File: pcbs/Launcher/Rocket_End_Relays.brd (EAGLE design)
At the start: 100 x 80 mm, 39 parts, among them IC2 LM2576T-ADJ, K4 LD105, K5 LD105, K6 LD105, K7 LD105, T1 BC547, T2 BC547, T3 BC547, T4 BC547, T5 BC547, U1 ARDUINO-MEGAPRO-5V, X1 22-23-2041, X2 22-23-2041, X3 22-23-2021, X4 22-23-2021, X5 22-23-2021, X7 22-23-2021

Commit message: * Added Arduino code for launcher code
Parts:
- R10: device resistor:0207/7 -> rcl:0207/7
- R13, R14: device rcl:0204/5 -> resistor:0207/7
- moved X4 25.4 mm to (52.1, 20.3)
- moved R3 11.5 mm to (63.5, 14.0)
- moved R13 6.35 mm to (8.89, 20.3), turned to 180 degrees
- moved C4 4.02 mm to (7.62, 14.0), turned to 270 degrees
- moved C3 2.84 mm to (8.89, 57.1), turned to 90 degrees
- moved X5 2.54 mm to (26.7, 17.8), turned to 270 degrees
- moved R14 1.27 mm to (11.4, 14.0)
- turned R10 to 270 degrees
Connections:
- removed net N$28: U1.5V@1, X1.3, X2.3
- net N$23: now also R12.2, U1.5V@1, X1.3, X2.3; no longer R12.1, T5.3
- net N$26: now also R12.1, T5.3; no longer R10.2, T5.1
- net N$31: now also R10.2
- net N$33: now also T5.1
- net N$5: no longer R12.2
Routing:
- net N$23: track 11.2 -> 57.0 mm, vias 0 -> 2
- net N$28: track 43.8 -> 0.00 mm
- net N$15: track 60.1 -> 34.7 mm
- net N$17: track 62.2 -> 39.7 mm
- net N$26: track 7.34 -> 16.9 mm
- net N$33: track 324.6 -> 315.2 mm, vias 6 -> 8
- net N$29: track 49.8 -> 44.5 mm
- net N$37: track 49.5 -> 44.2 mm
- net N$31: track 11.8 -> 15.6 mm
- net N$3: track 26.7 -> 23.4 mm
- net N$5: track 195.3 -> 192.7 mm
- net N$30: track 25.6 -> 24.2 mm
- net VCC: track 110.7 -> 111.4 mm

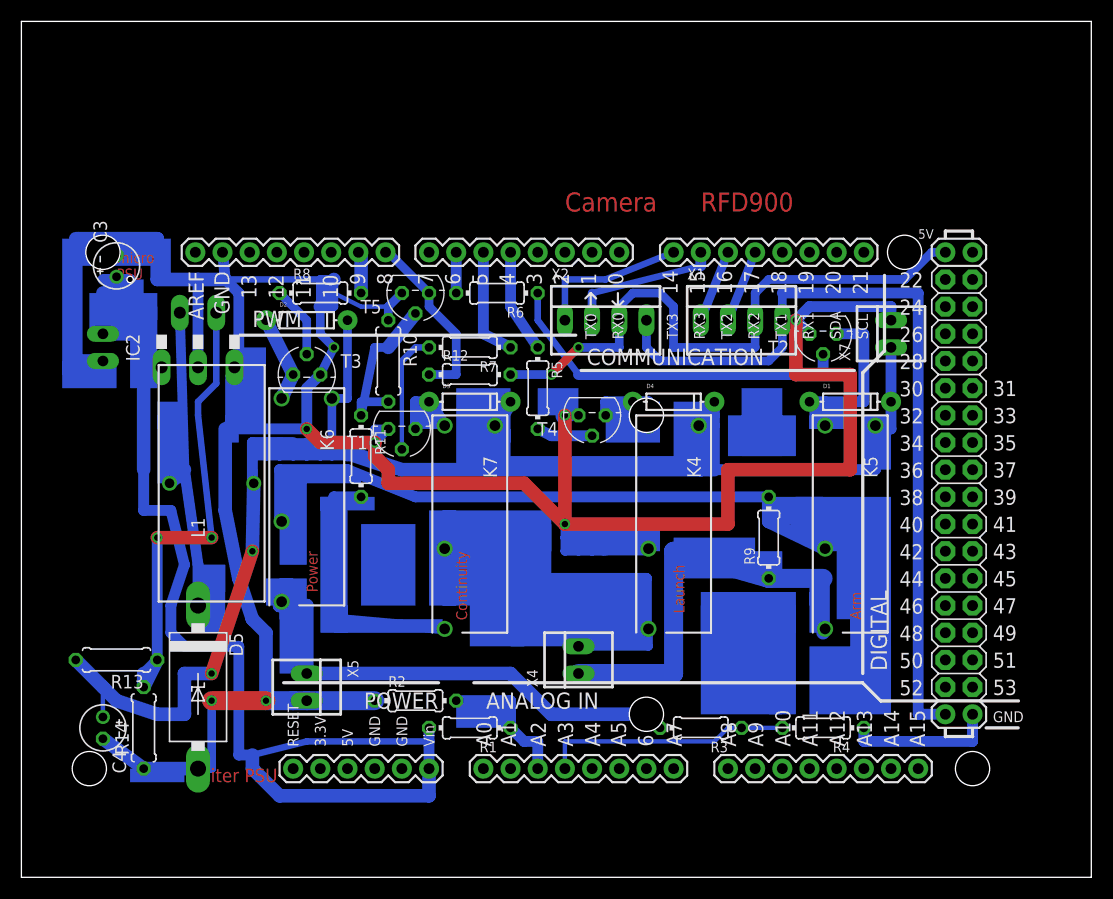
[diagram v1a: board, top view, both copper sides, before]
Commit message: * Cleaning up board with curved tracks * Putting in two screw in terminal blocks for Igniter PSU   and wires to igniter!
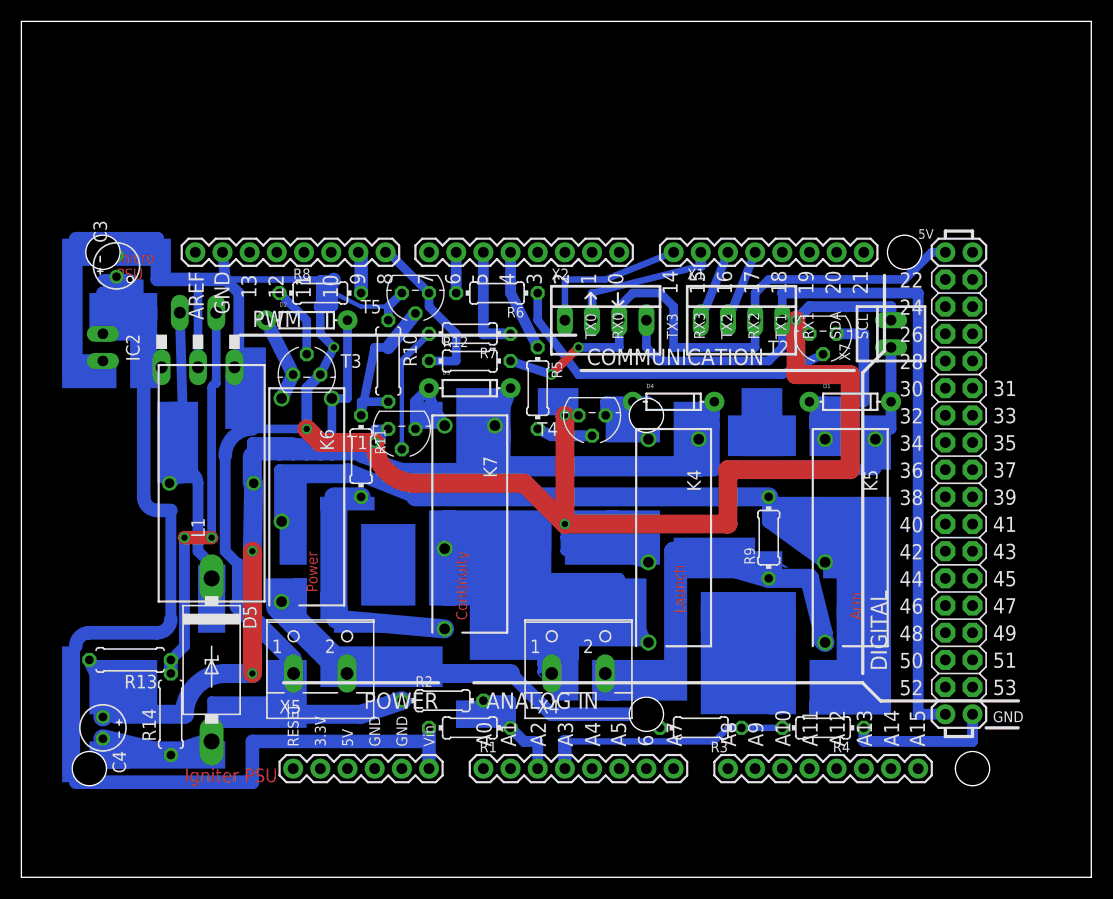
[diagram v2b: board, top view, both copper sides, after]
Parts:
- X4, X5: value 22-23-2021 -> (none); device con-molex:22-23-2021 -> con-wago-500:W237-102
- moved R14 2.84 mm to (14.0, 15.2)
- moved D5 2.84 mm to (17.8, 20.3)
- moved X5 2.84 mm to (27.9, 20.3), turned to 0 degrees
- moved R2 2.54 mm to (39.4, 16.5)
- moved K4 1.27 mm to (61.0, 31.8)
- moved K5 1.27 mm to (77.5, 31.8)
- moved R13 1.27 mm to (10.2, 20.3)
- moved D3 1.27 mm to (41.9, 45.7)
- moved R12 1.27 mm to (41.9, 48.3)
- moved R7 1.27 mm to (41.9, 50.8)
- turned X4 to 0 degrees
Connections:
- net N$15: now also X4.1; no longer X4.2
- net N$17: now also X4.2; no longer X4.1
- net N$29: now also X5.2; no longer X5.1
- net N$33: now also X5.1; no longer X5.2
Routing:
- net N$37: track 44.2 -> 37.0 mm
- net N$28: track 0.00 -> 4.86 mm
- net N$29: track 44.5 -> 40.8 mm
- net N$17: track 39.7 -> 37.1 mm
- net N$5: track 192.7 -> 195.3 mm
- net N$7: track 13.2 -> 10.7 mm
- net N$20: track 6.57 -> 8.19 mm
- net N$36: track 29.4 -> 27.8 mm
- net N$10: track 33.7 -> 32.2 mm
- net N$33: track 315.2 -> 313.9 mm, vias 8 -> 5
- net N$26: track 16.9 -> 15.6 mm
- net N$22: track 17.7 -> 18.9 mm
- net N$19: track 7.50 -> 8.77 mm
- net N$15: track 34.7 -> 33.8 mm
- net VCC: track 111.4 -> 112.1 mm
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- added copper zone on layer 16, net N$35
- added copper zone on layer 16, net N$38
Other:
- board text removed: "Camera"
- board text removed: "RFD900"

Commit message: * Labelling added to screw terminal blocks
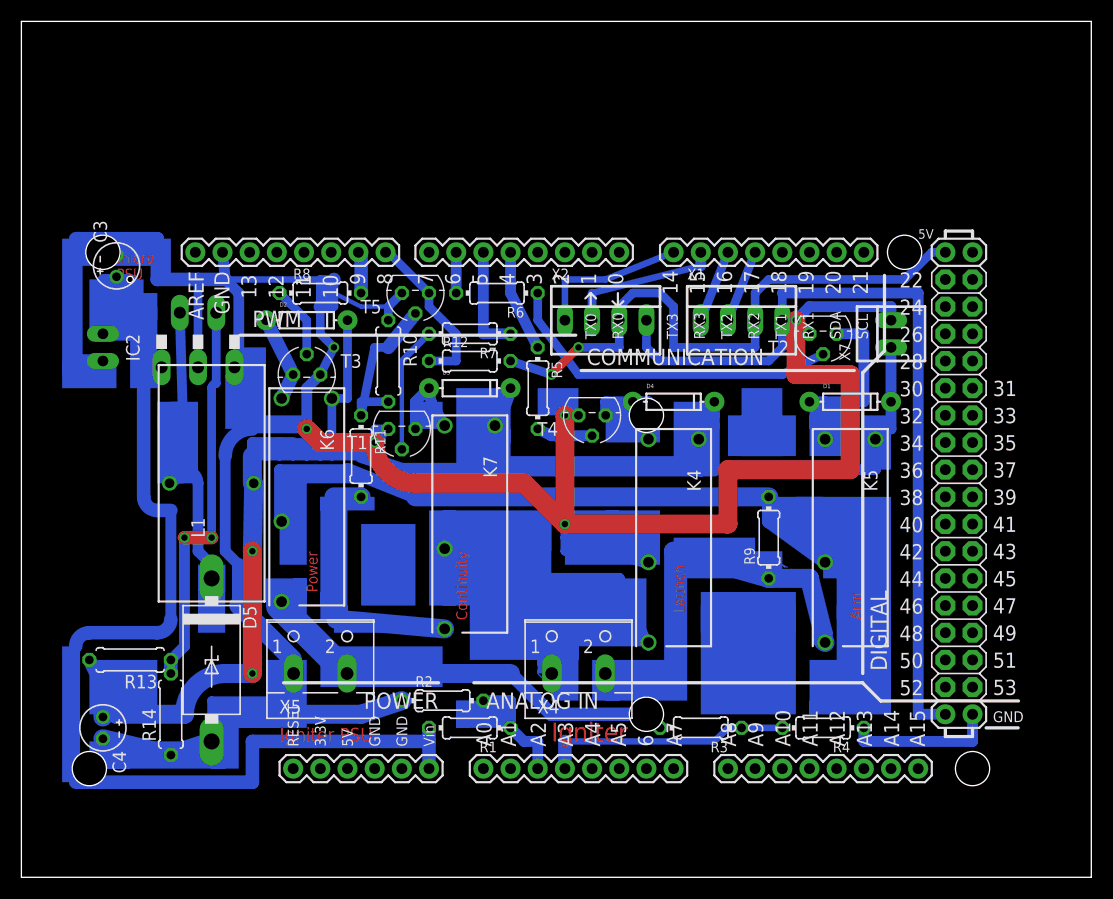
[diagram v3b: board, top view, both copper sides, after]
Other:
- board text added: "Igniter"
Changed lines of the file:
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@@
 <text x="60.96" y="29.21" size="1.016" layer="1" rot="R270">Launch</text>
 <text x="40.64" y="30.48" size="1.016" layer="1" rot="R270">Continuity</text>
-<text x="15.24" y="8.89" size="1.27" layer="1">Igniter PSU</text>
+<text x="24.13" y="12.7" size="1.27" layer="1">Igniter PSU</text>
 <text x="8.89" y="55.88" size="1.016" layer="1">micro
 PSU</text>
@@
 <rectangle x1="22.86" y1="25.4" x2="26.67" y2="27.94" layer="16"/>
 <rectangle x1="25.4" y1="24.13" x2="26.67" y2="27.94" layer="16"/>
+<rectangle x1="17.78" y1="10.16" x2="19.05" y2="15.24" layer="16"/>
+<rectangle x1="17.78" y1="10.16" x2="20.32" y2="15.24" layer="16"/>
+<text x="49.53" y="12.7" size="1.778" layer="1">Igniter</text>
+<rectangle x1="21.59" y1="41.91" x2="26.67" y2="43.18" layer="16"/>
+<rectangle x1="6.35" y1="54.61" x2="7.62" y2="55.88" layer="16"/>
 </plain>
 <attributes>
@@
 <wire x1="13.97" y1="24.13" x2="12.7" y2="22.86" width="1.27" layer="16" curve="-90"/>
 <wire x1="12.7" y1="22.86" x2="6.35" y2="22.86" width="1.27" layer="16"/>
-<wire x1="5.08" y1="20.32" x2="5.08" y2="8.89" width="0" layer="19" extent="1-16"/>
 <wire x1="6.35" y1="22.86" x2="5.08" y2="21.59" width="1.27" layer="16" curve="90"/>
 <wire x1="5.08" y1="21.59" x2="5.08" y2="8.89" width="0.8128" layer="16"/>

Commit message: * Making more trackers thicker and nicer.
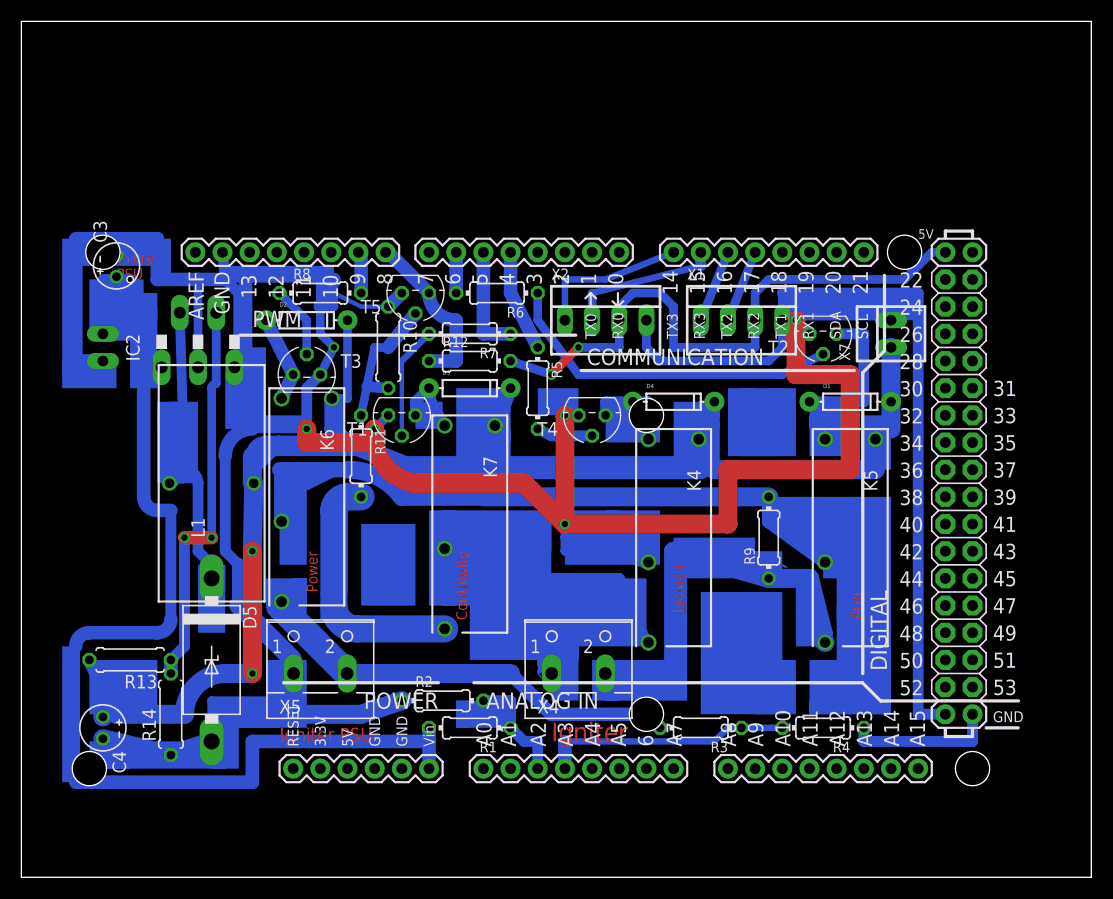
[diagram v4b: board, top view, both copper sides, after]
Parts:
- moved R10 1.27 mm to (34.3, 49.5)
- moved T1 1.27 mm to (35.6, 43.2)
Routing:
- net N$5: track 195.3 -> 168.6 mm
- net N$25: track 59.9 -> 73.7 mm
- net N$31: track 15.6 -> 13.8 mm
- net N$33: track 313.9 -> 312.3 mm
- net N$20: track 8.19 -> 6.92 mm
- net N$13: track 11.8 -> 10.6 mm

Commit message: * Trying to increase width of particular tracks * Putting in curve tracks to neaten up some areas * Putting in resistor and diode values.
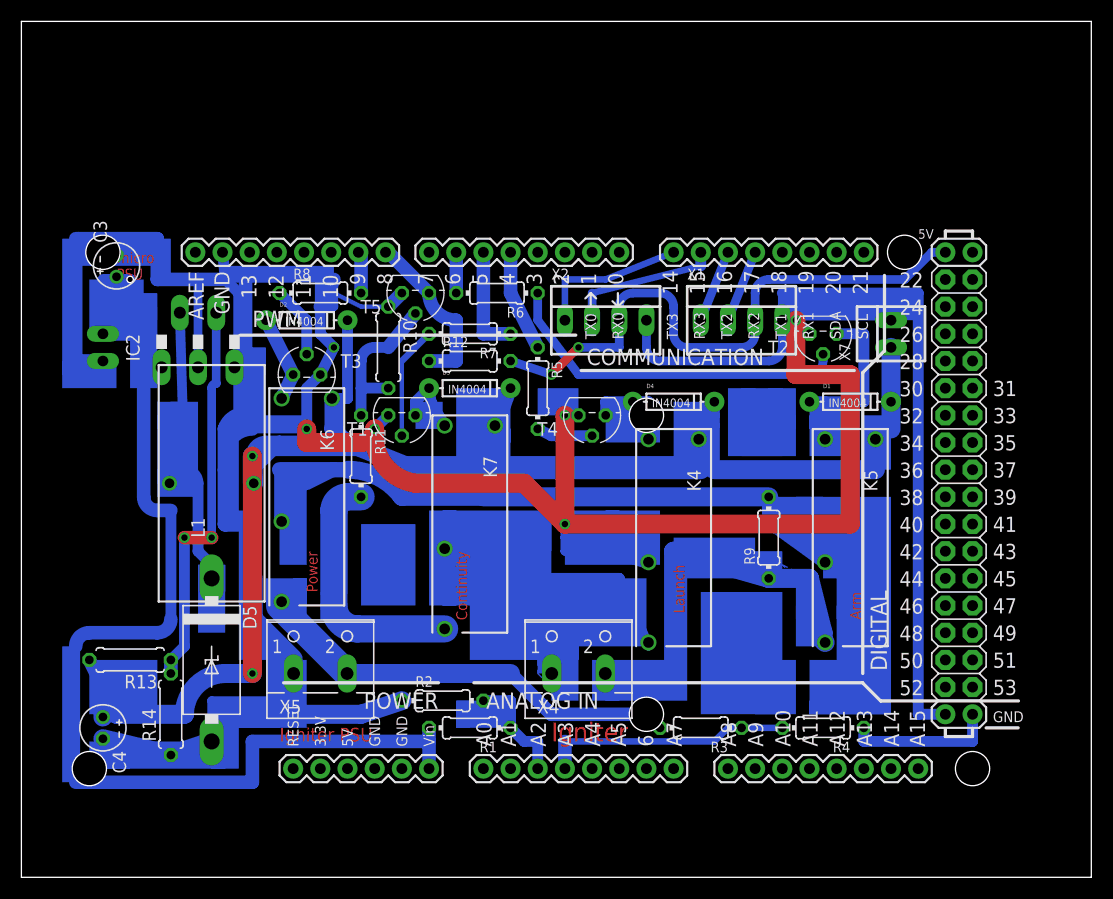
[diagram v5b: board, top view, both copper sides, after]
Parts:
- C3: value (none) -> 100uF 16V
- C4: value (none) -> 330uF 16V
- D1, D2, D3, D4: value (none) -> IN4004
- D5: value 1N5908 -> 1N5822
- L1: value (none) -> 100uH 3Amp
- R1: value (none) -> 15k
- R10, R12, R3, R9: value (none) -> 10k
- R11, R6, R7, R8: value (none) -> 1k
- R13, R2, R4: value (none) -> 4.7k
- R14: value (none) -> 1.5k
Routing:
- net N$33: track 312.3 -> 320.4 mm
- net N$5: track 168.6 -> 171.1 mm
- net N$23: track 57.2 -> 55.7 mm
- net N$31: track 13.8 -> 14.8 mm
- net N$10: track 32.2 -> 32.9 mm

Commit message: * Added library deps * Modified to use an edited version of library, removing most of digital pins * adding in connector pins to put right angle 2 lots of 2x4 pins
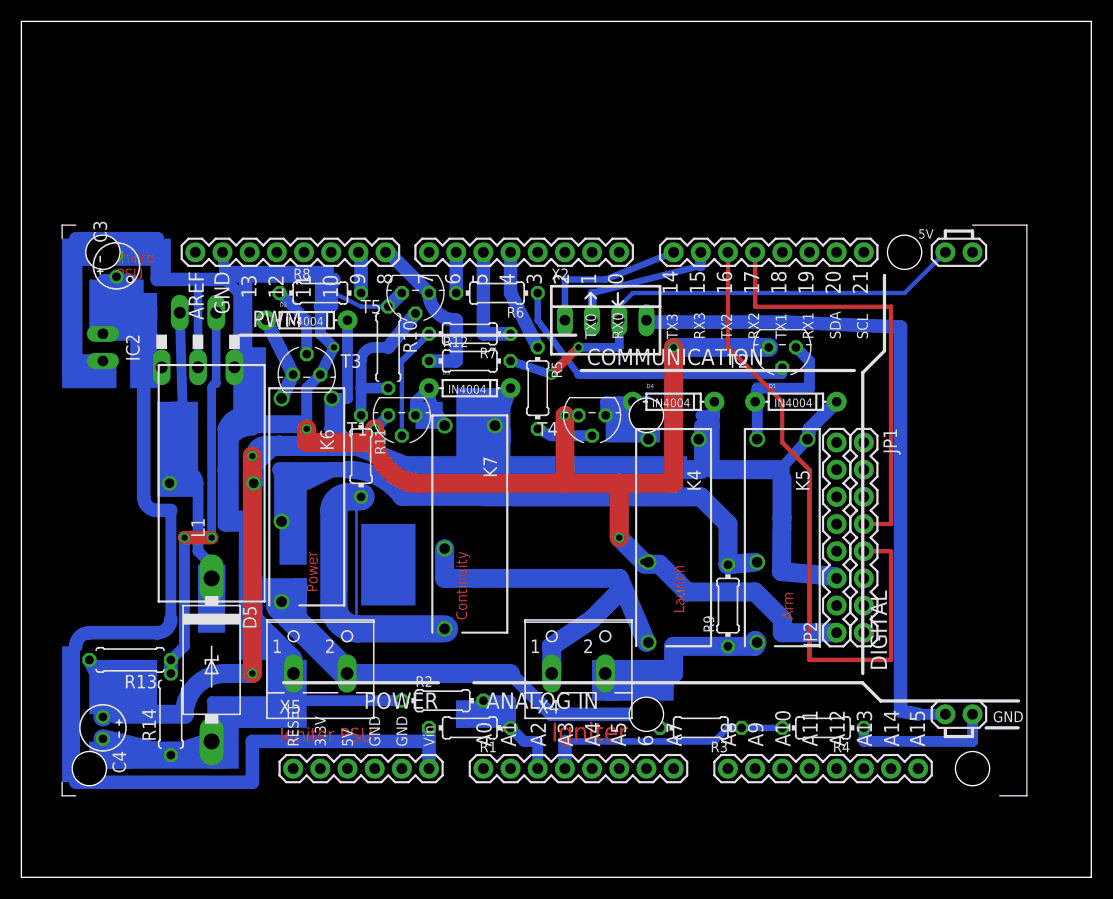
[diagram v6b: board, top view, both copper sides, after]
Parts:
- removed X1: 22-23-2041, con-molex:22-23-2041
- removed X7: 22-23-2021, con-molex:22-23-2021
- added JP1, JP2: (no value), SparkFun-Connectors:1X08_ROUND
- U1: device SparkFun-Boards:ARDUINO_MEGA-PRO-5V -> JoeMega_Ether_Edited:ARDUINO_MEGA-PRO-5V
- moved R9 7.41 mm to (66.0, 25.4)
- moved K5 6.35 mm to (71.1, 31.8)
- moved D1 5.08 mm to (72.4, 44.5)
- moved T2 4.02 mm to (71.1, 49.5)
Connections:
- net N$1: now also JP1.5; no longer X1.1
- net N$16: no longer X1.4
- net N$2: now also JP1.4; no longer X1.2
- net N$23: no longer X1.3
- net N$33: now also JP2.1; no longer X7.2
- net N$5: now also JP2.3; no longer X7.1
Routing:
- net N$1: track 6.84 -> 61.6 mm
- net N$33: track 320.4 -> 281.8 mm, vias 5 -> 7
- net N$2: track 6.84 -> 40.6 mm
- net N$17: track 37.1 -> 17.4 mm
- net N$30: track 24.5 -> 36.8 mm
- net N$16: track 76.0 -> 64.1 mm
- net N$23: track 55.7 -> 47.8 mm
- net N$25: track 73.7 -> 68.6 mm
- net N$28: track 4.86 -> 0.00 mm
- net N$15: track 33.8 -> 38.5 mm
- net N$10: track 32.9 -> 28.6 mm
- net N$22: track 18.9 -> 15.3 mm
- net N$34: track 3.07 -> 0.00 mm
- net N$5: track 171.1 -> 173.7 mm
- removed copper zone on layer 16, net N$35
- removed copper zone on layer 16, net N$38
